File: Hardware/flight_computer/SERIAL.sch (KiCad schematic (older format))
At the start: 2 parts, among them U3001 TXS0108ERGYR, U3002 TXS0108ERGYR

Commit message: added parts for DAN <3
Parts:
- U3001, U3002: symbol openDrone_parts:TXS0108ERGYR -> flight_computer-rescue:TXS0108ERGYR-openDrone_parts
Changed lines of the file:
@@
 $EndDescr
 $Comp
-L openDrone_parts:TXS0108ERGYR U3002
+L flight_computer-rescue:TXS0108ERGYR-openDrone_parts U3002
 U 1 1 5F61A29E
 P 1700 1650
@@
 	1700 1850 1450 1850
 $Comp
-L openDrone_parts:TXS0108ERGYR U3001
+L flight_computer-rescue:TXS0108ERGYR-openDrone_parts U3001
 U 1 1 5F61C67F
 P 1700 3900

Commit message: added more parts and datasheets
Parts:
- U3001, U3002: symbol flight_computer-rescue:TXS0108ERGYR-openDrone_parts -> flight_computer-rescue:TXS0108ERGYR-openDrone_parts-flight_computer-rescue
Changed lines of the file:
@@
 $EndDescr
 $Comp
-L flight_computer-rescue:TXS0108ERGYR-openDrone_parts U3002
+L flight_computer-rescue:TXS0108ERGYR-openDrone_parts-flight_computer-rescue U3002
 U 1 1 5F61A29E
 P 1700 1650
@@
 	1700 1850 1450 1850
 $Comp
-L flight_computer-rescue:TXS0108ERGYR-openDrone_parts U3001
+L flight_computer-rescue:TXS0108ERGYR-openDrone_parts-flight_computer-rescue U3001
 U 1 1 5F61C67F
 P 1700 3900

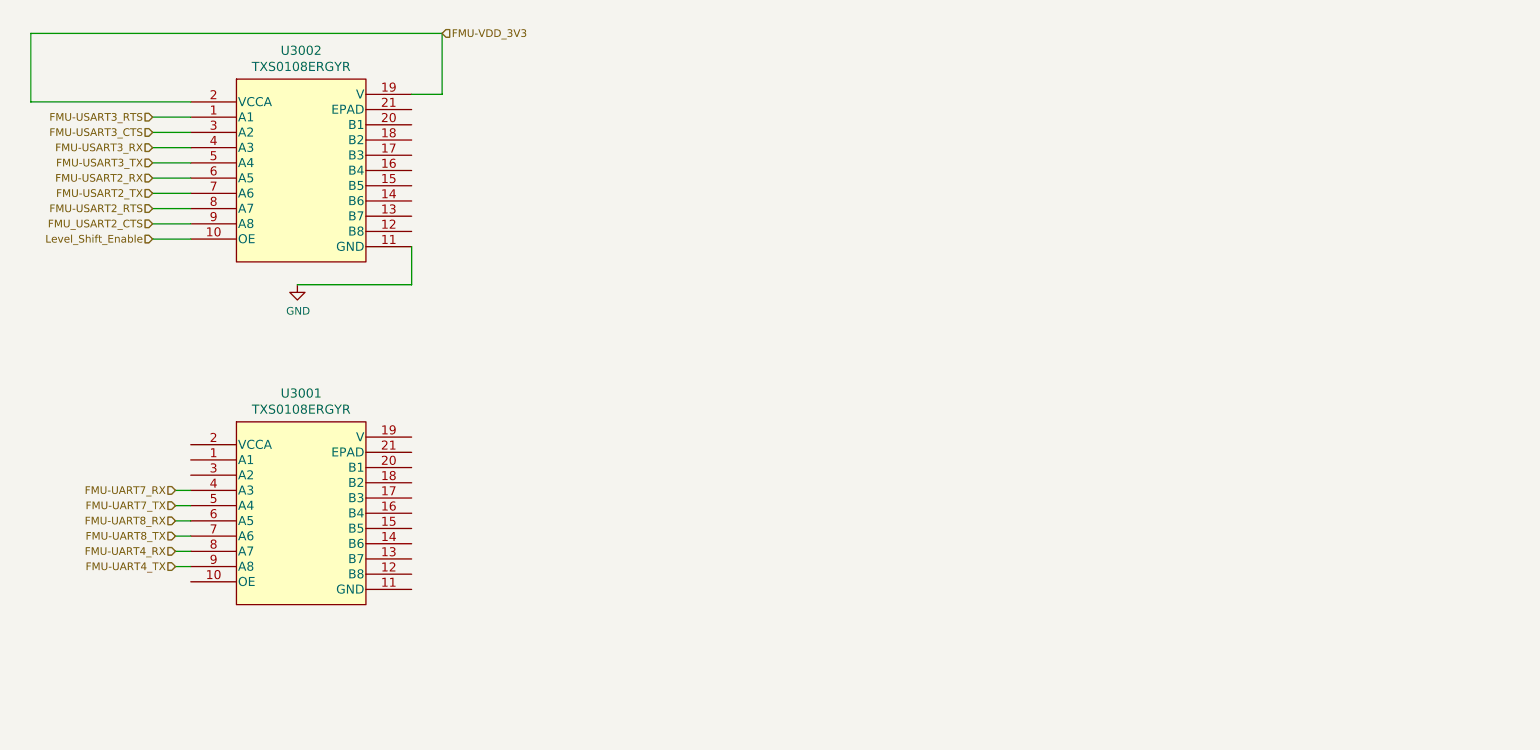
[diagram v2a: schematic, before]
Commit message: Updates SD-USB and SERIAL schematics
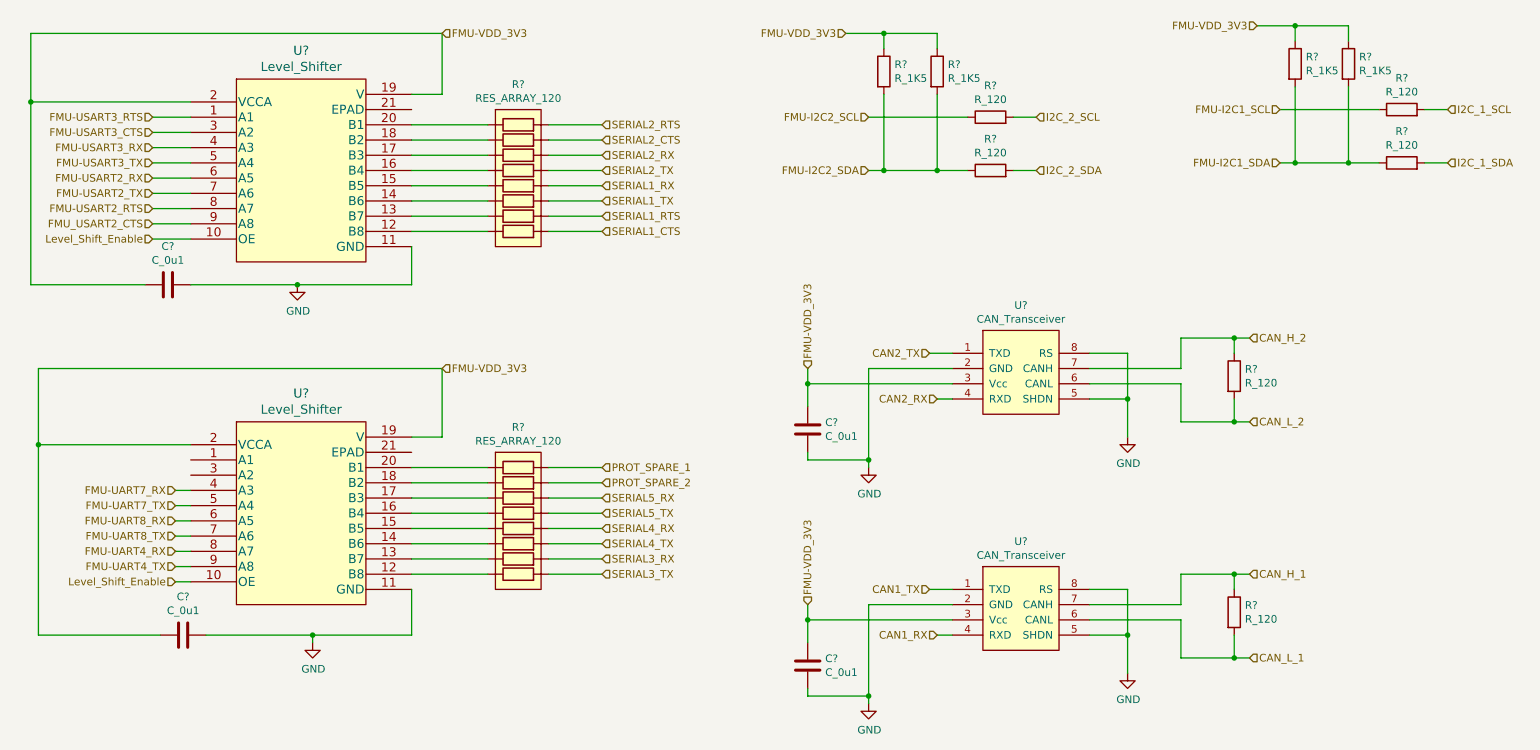
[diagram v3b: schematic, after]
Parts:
- removed U3001, U3002: TXS0108ERGYR, RGY20_3P05X2P05, symbol flight_computer-rescue:TXS0108ERGYR-openDrone_parts-flight_computer-rescue
- added C? (x4): C_0u1, Capacitors_SMD:C_0805, symbol openDrone_parts:C_0u1
- added R? (x6): R_120, Resistors_SMD:R_0805, symbol openDrone_parts:R_120
- added R? (x4): R_1K5, Resistors_SMD:R_0805, symbol openDrone_parts:R_1K5
- added R? (x2): RES_ARRAY_120, drone_footprints:EXB-2HV104JV, symbol openDrone_parts:RES_ARRAY_120
- added U? (x2): Level_Shifter, drone_footprints:TXS0108ERGYR, symbol openDrone_parts:Level_Shifter
- added U? (x2): CAN_Transceiver, TO_SOT_Packages_SMD:SOT-23-8, symbol openDrone_parts:CAN_Transceiver
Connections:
- net FMU-UART4_RX: now also U?.8 (A7)
- net FMU-UART4_TX: now also U?.9 (A8)
- net FMU-UART7_RX: now also U?.4 (A3)
- net FMU-UART7_TX: now also U?.5 (A4)
- net FMU-UART8_RX: now also U?.6 (A5)
- net FMU-UART8_TX: now also U?.7 (A6)
- net FMU-USART2_RTS: now also U?.8 (A7)
- net FMU-USART2_RX: now also U?.6 (A5)
- net FMU-USART2_TX: now also U?.7 (A6)
- net FMU-USART3_CTS: now also U?.3 (A2)
- net FMU-USART3_RTS: now also U?.1 (A1)
- net FMU-USART3_RX: now also U?.4 (A3)
- net FMU-USART3_TX: now also U?.5 (A4)
- net FMU-VDD_3V3: now also C?.1, C?.1, C?.1, C?.1, R?.1, R?.1, R?.1, R?.1, U?.19 (V), U?.19 (V), U?.2 (VCCA), U?.2 (VCCA), U?.3 (Vcc), U?.3 (Vcc)
- net FMU_USART2_CTS: now also U?.9 (A8)
- net GND: now also C?.2, C?.2, C?.2, C?.2, U?.11 (GND), U?.11 (GND), U?.2 (GND), U?.2 (GND), U?.5 (SHDN), U?.5 (SHDN), U?.8 (RS), U?.8 (RS)
- net Level_Shift_Enable: now also U?.10 (OE), U?.10 (OE)
- new net: R?.8, U?.12 (B8) (x2)
- new net: R?.7, U?.13 (B7) (x2)
- new net: R?.6, U?.14 (B6) (x2)
- new net: R?.5, U?.15 (B5) (x2)
- new net: R?.4, U?.16 (B4) (x2)
- new net: R?.3, U?.17 (B3) (x2)
- new net: R?.2, U?.18 (B2) (x2)
- new net: R?.1, U?.20 (B1) (x2)
- new net CAN1_RX: U?.4 (RXD)
- new net CAN1_TX: U?.1 (TXD)
- new net CAN2_RX: U?.4 (RXD)
- new net CAN2_TX: U?.1 (TXD)
- new net CAN_H_1: R?.1, U?.7 (CANH)
- new net CAN_H_2: R?.1, U?.7 (CANH)
- new net CAN_L_1: R?.2, U?.6 (CANL)
- new net CAN_L_2: R?.2, U?.6 (CANL)
- new net FMU-I2C1_SCL: R?.1
- new net FMU-I2C1_SDA: R?.1, R?.2, R?.2
- new net FMU-I2C2_SCL: R?.1
- new net FMU-I2C2_SDA: R?.1, R?.2, R?.2
- new net I2C_1_SCL: R?.2
- new net I2C_1_SDA: R?.2
- new net I2C_2_SCL: R?.2
- new net I2C_2_SDA: R?.2
- new net PROT_SPARE_1: R?.16
- new net PROT_SPARE_2: R?.15
- new net SERIAL1_CTS: R?.9
- new net SERIAL1_RTS: R?.10
- new net SERIAL1_RX: R?.12
- new net SERIAL1_TX: R?.11
- new net SERIAL2_CTS: R?.15
- new net SERIAL2_RTS: R?.16
- new net SERIAL2_RX: R?.14
- new net SERIAL2_TX: R?.13
- new net SERIAL3_RX: R?.10
- new net SERIAL3_TX: R?.9
- new net SERIAL4_RX: R?.12
- new net SERIAL4_TX: R?.11
- new net SERIAL5_RX: R?.14
- new net SERIAL5_TX: R?.13
